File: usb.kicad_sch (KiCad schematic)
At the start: 3 parts, among them J6 47590-0001, U6 USBLC6-2SC6

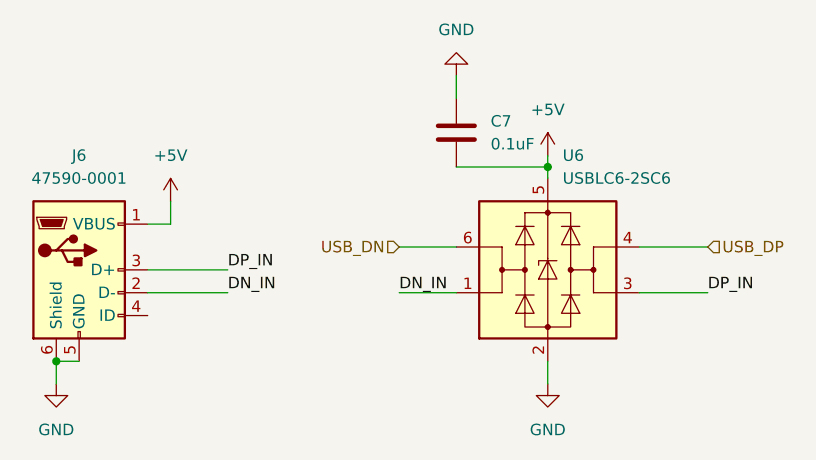
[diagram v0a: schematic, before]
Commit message: Added JLPCB DRCs, antenna hatching
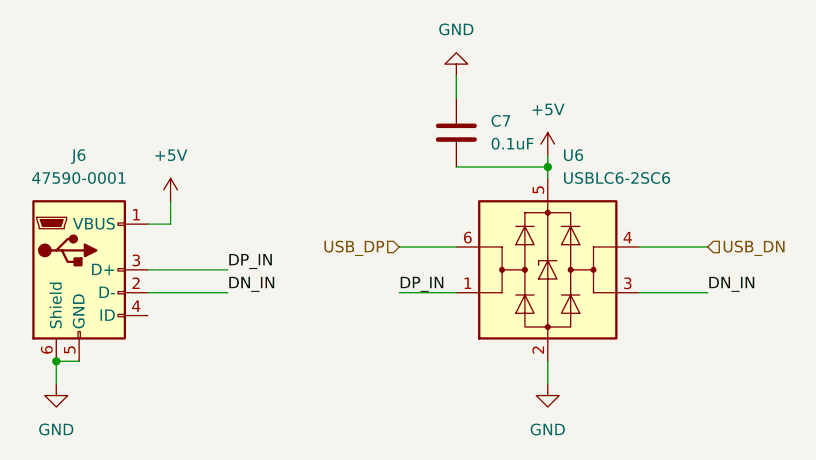
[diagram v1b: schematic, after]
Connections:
- net DN_IN: now also U6.3 (I/O2); no longer U6.1 (I/O1)
- net DP_IN: now also U6.1 (I/O1); no longer U6.3 (I/O2)
- net USB_DN: now also U6.4 (I/O2); no longer U6.6 (I/O1)
- net USB_DP: now also U6.6 (I/O1); no longer U6.4 (I/O2)
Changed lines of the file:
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@@
     (effects (font (size 1.27 1.27)) (justify left bottom))
   )
-  (label "DP_IN" (at 166.37 82.55 0) (fields_autoplaced)
+  (label "DN_IN" (at 166.37 82.55 0) (fields_autoplaced)
     (effects (font (size 1.27 1.27)) (justify left bottom))
   )
@@
     (effects (font (size 1.27 1.27)) (justify left bottom))
   )
-  (label "DN_IN" (at 132.08 82.55 0) (fields_autoplaced)
+  (label "DP_IN" (at 132.08 82.55 0) (fields_autoplaced)
     (effects (font (size 1.27 1.27)) (justify left bottom))
   )
-  (hierarchical_label "USB_DN" (shape input) (at 132.08 77.47 180) (fields_autoplaced)
+  (hierarchical_label "USB_DP" (shape input) (at 132.08 77.47 180) (fields_autoplaced)
     (effects (font (size 1.27 1.27)) (justify right))
   )
-  (hierarchical_label "USB_DP" (shape input) (at 166.37 77.47 0) (fields_autoplaced)
+  (hierarchical_label "USB_DN" (shape input) (at 166.37 77.47 0) (fields_autoplaced)
     (effects (font (size 1.27 1.27)) (justify left))
   )

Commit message: Field updates, generating fab files
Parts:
- C7: value 0.1uF -> 0.1uF 20%; JLCPCB Part # (none) -> C359190
- J6: JLCPCB Part # (none) -> C136001
- U6: JLCPCB Part # (none) -> C5250994
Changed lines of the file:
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@@
       (effects (font (size 1.27 1.27)) (justify left))
     )
-    (property "Value" "0.1uF" (at 142.24 66.04 0)
+    (property "Value" "0.1uF 20%" (at 142.24 66.04 0)
       (effects (font (size 1.27 1.27)) (justify left))
     )
@@
       (effects (font (size 1.27 1.27)) hide)
     )
-    (property "Datasheet" "~" (at 138.43 64.77 0)
+    (property "Datasheet" "https://www.lcsc.com/product-detail/Multilayer-Ceramic-Capacitors-MLCC-SMD-SMT_CCTC-TCC0402X5R104M250AT_C359190.html" (at 138.43 64.77 0)
+      (effects (font (size 1.27 1.27)) hide)
+    )
+    (property "JLCPCB Part #" "C359190" (at 138.43 64.77 0)
       (effects (font (size 1.27 1.27)) hide)
     )
@@
       (effects (font (size 1.27 1.27)) hide)
     )
-    (property "Datasheet" "~" (at 100.33 81.28 0)
+    (property "Datasheet" "https://www.lcsc.com/product-detail/USB-Connectors_MOLEX-475900001_C136001.html" (at 100.33 81.28 0)
+      (effects (font (size 1.27 1.27)) hide)
+    )
+    (property "JLCPCB Part #" "C136001" (at 96.52 80.01 0)
       (effects (font (size 1.27 1.27)) hide)
     )
@@
       (effects (font (size 1.27 1.27)) hide)
     )
+    (property "JLCPCB Part #" "C5250994" (at 148.59 80.01 0)
+      (effects (font (size 1.27 1.27)) hide)
+    )

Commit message: Changed outline for DFM
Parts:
- C7: JLCPCB Part # C359190 -> (none); LCSC (none) -> C359190
- J6: JLCPCB Part # C136001 -> (none); LCSC (none) -> C136001
- U6: JLCPCB Part # C5250994 -> (none); LCSC (none) -> C5250994
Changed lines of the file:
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@@
       (effects (font (size 1.27 1.27)) hide)
     )
-    (property "JLCPCB Part #" "C359190" (at 138.43 64.77 0)
+    (property "LCSC" "C359190" (at 138.43 64.77 0)
       (effects (font (size 1.27 1.27)) hide)
     )
@@
       (effects (font (size 1.27 1.27)) hide)
     )
-    (property "JLCPCB Part #" "C136001" (at 96.52 80.01 0)
+    (property "LCSC" "C136001" (at 96.52 80.01 0)
       (effects (font (size 1.27 1.27)) hide)
     )
@@
       (effects (font (size 1.27 1.27)) hide)
     )
-    (property "JLCPCB Part #" "C5250994" (at 148.59 80.01 0)
+    (property "LCSC" "C5250994" (at 148.59 80.01 0)
       (effects (font (size 1.27 1.27)) hide)
     )
